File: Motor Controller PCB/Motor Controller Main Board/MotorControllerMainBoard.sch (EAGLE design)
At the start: 55 parts, among them T1 TEENSY_3.1_ALL_PINS

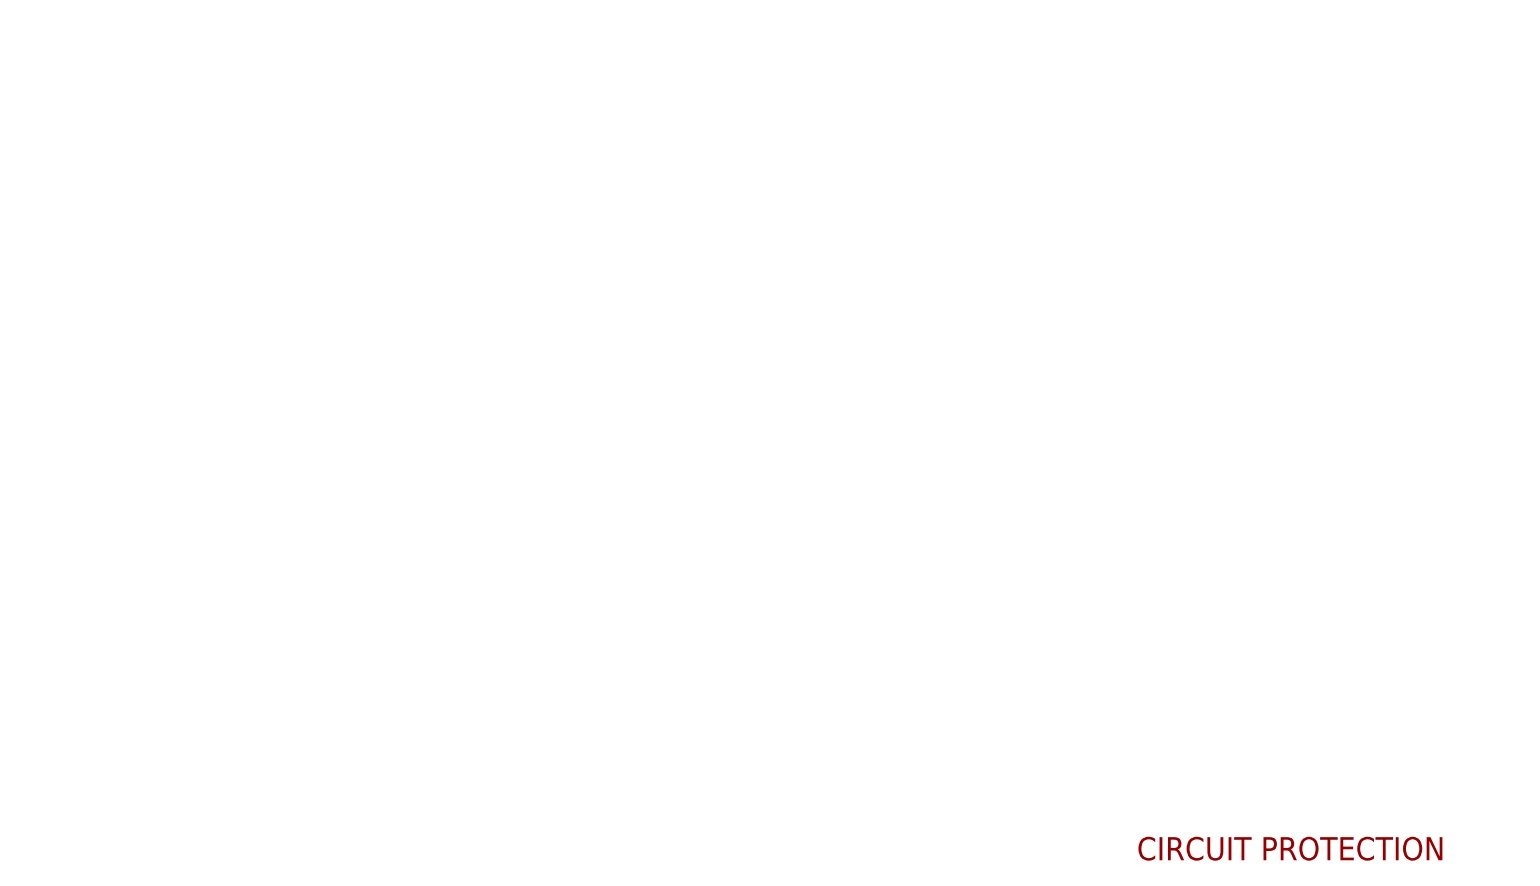
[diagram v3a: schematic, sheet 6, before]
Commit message: Added input filter Capacitors.
3.4mF of input capacitance that has very low effective series resistance
and inductance.
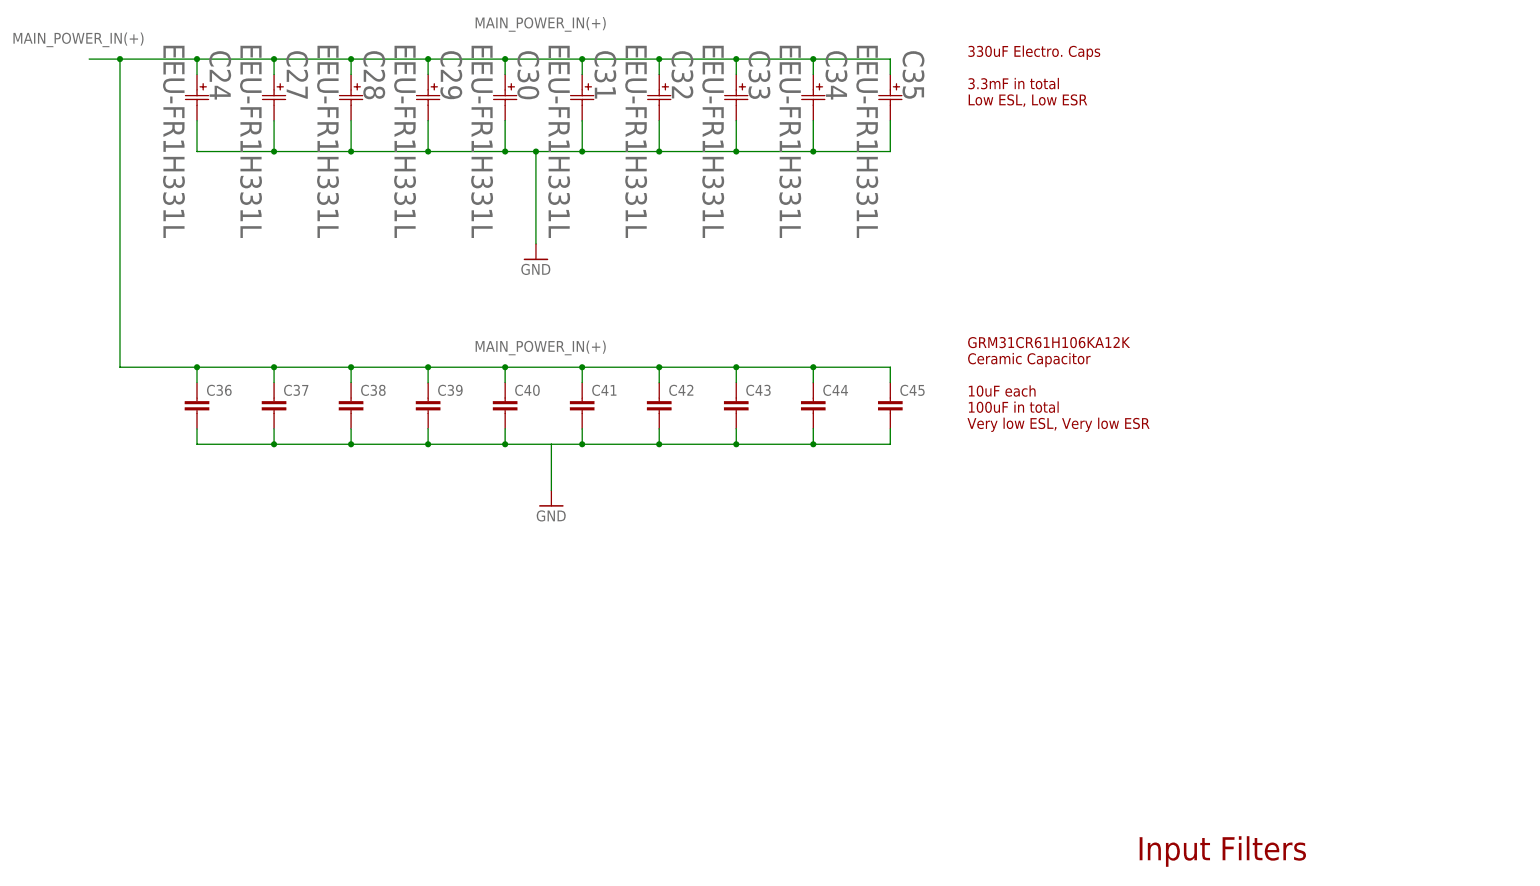
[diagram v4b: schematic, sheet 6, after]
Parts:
- added C24, C27, C28, C29, C30, C31, C32, C33, C34, C35: EEU-FR1H331L, MotorControllerEagleLibrary:EEU-FR1H331L
- added C36, C37, C38, C39, C40, C41, C42, C43, C44, C45: (no value), resistor:C-EUC1206
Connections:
- net GND: now also C24.22, C27.22, C28.22, C29.22, C30.22, C31.22, C32.22, C33.22, C34.22, C35.22, C36.2, C37.2, C38.2, C39.2, C40.2, C41.2, C42.2, C43.2, C44.2, C45.2
- net MAIN_POWER_IN(+): now also C24.11, C27.11, C28.11, C29.11, C30.11, C31.11, C32.11, C33.11, C34.11, C35.11, C36.1, C37.1, C38.1, C39.1, C40.1, C41.1, C42.1, C43.1, C44.1, C45.1
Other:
- note added: "330uF Electro. Caps 3.3mF in total Low ESL, Low ESR"
- note added: "GRM31CR61H106KA12K Ceramic Capacitor 10uF each 100uF in total Very low ESL, Very low ESR"
- note added: "Input Filters"
- note added: "On Board Filters"
- note removed: "CIRCUIT PROTECTION"
- note removed: "Circuit Protection - Overvoltage - Reverse Polarity"

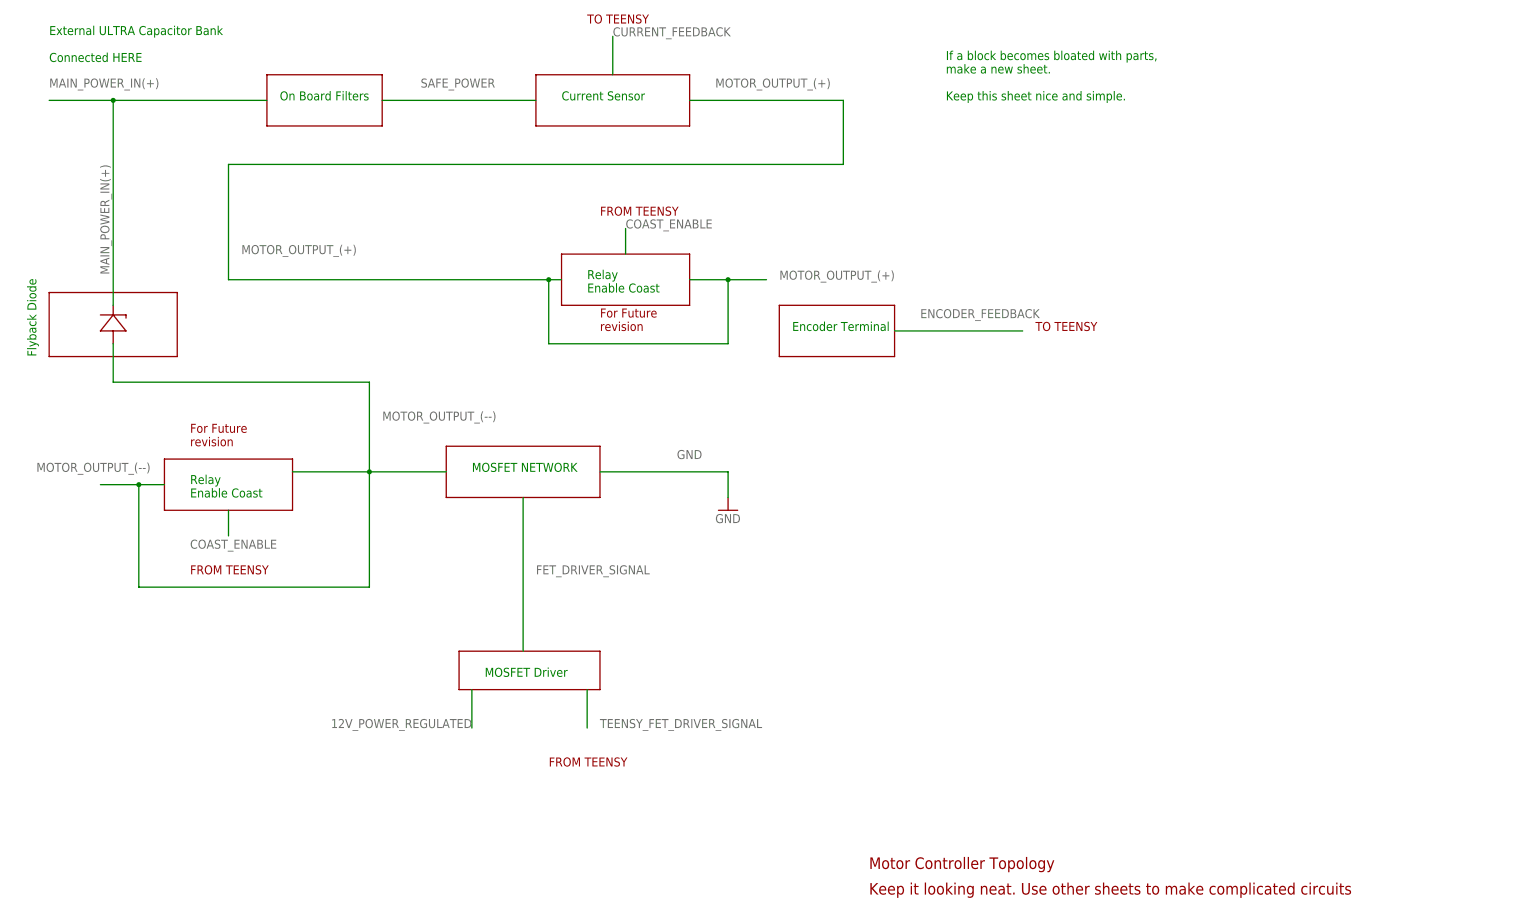
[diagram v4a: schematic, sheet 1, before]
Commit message: Added Screw Terminals to Schematic
-Added library for the screw terminal
-Added Power terminals and Motor terminals
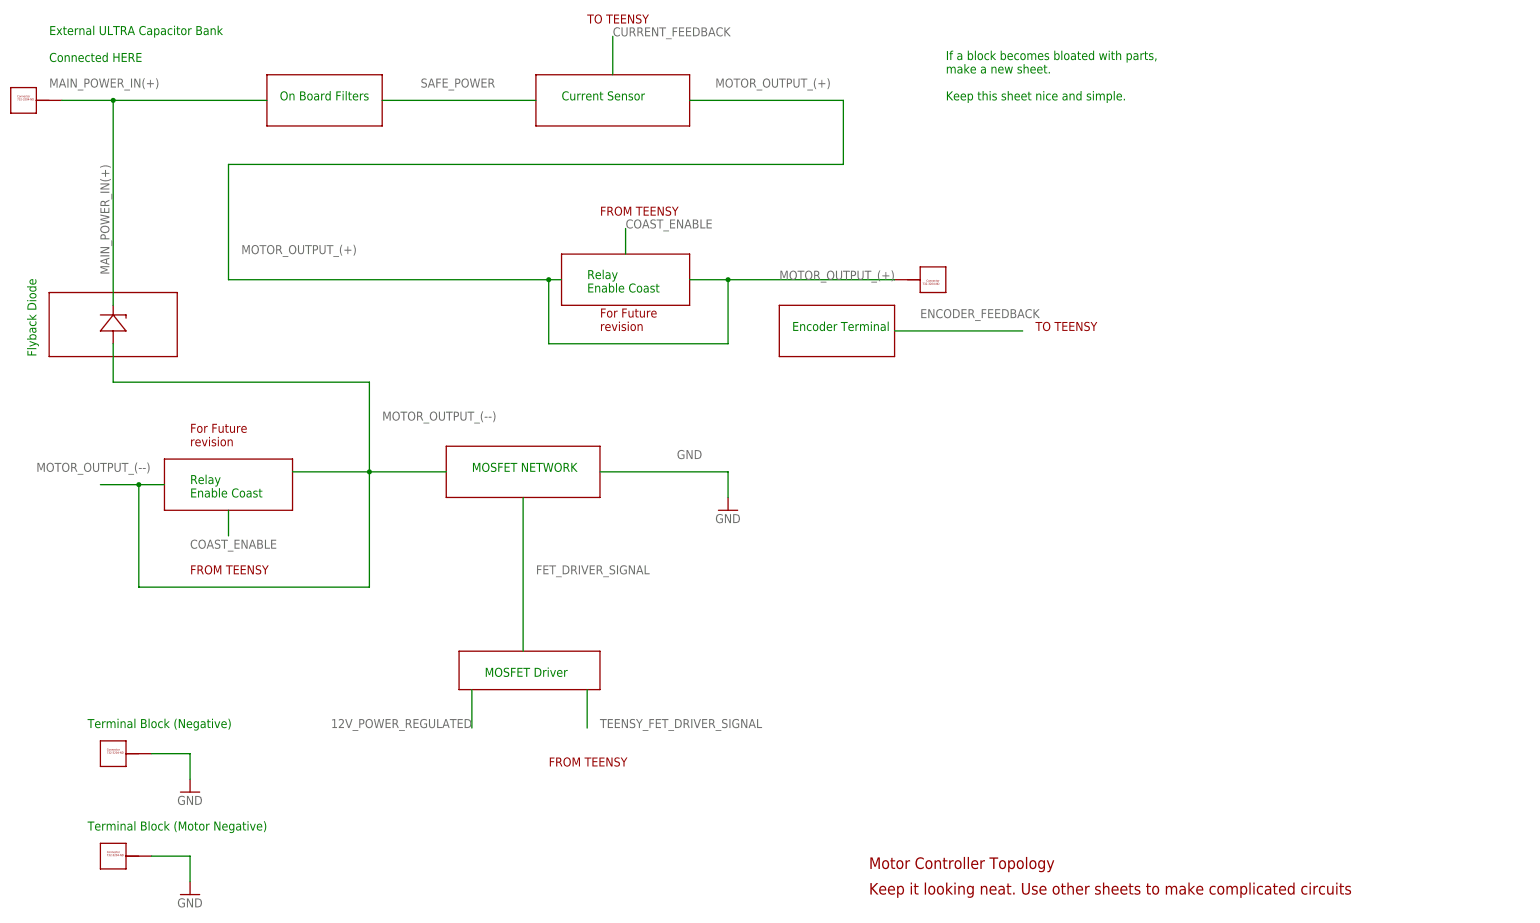
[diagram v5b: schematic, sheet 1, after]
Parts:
- added U$12, U$14, U$15, U$16: 732-3204-ND_CONNECTOR, Connector 732-3204:732-3204-ND_CONNECTOR
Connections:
- net GND: now also U$14.P$1
- net MAIN_POWER_IN(+): now also U$12.P$1
- net MOTOR_OUTPUT_(+): now also U$15.P$1
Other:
- note added: "Terminal Block (Motor Negative)"
- note added: "Terminal Block (Negative)"
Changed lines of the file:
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@@
 <part name="C45" library="resistor" deviceset="C-EU" device="C1206"/>
 <part name="GND25" library="SparkFun-Aesthetics" deviceset="GND" device=""/>
+<part name="U$12" library="Connector 732-3204" deviceset="732-3204-ND_CONNECTOR" device=""/>
+<part name="U$14" library="Connector 732-3204" deviceset="732-3204-ND_CONNECTOR" device=""/>
+<part name="GND26" library="E-P-008-R1.2" deviceset="GND" device=""/>
+<part name="U$15" library="Connector 732-3204" deviceset="732-3204-ND_CONNECTOR" device=""/>
+<part name="U$16" library="Connector 732-3204" deviceset="732-3204-ND_CONNECTOR" device=""/>
+<part name="GND27" library="E-P-008-R1.2" deviceset="GND" device=""/>
 </parts>
 <sheets>
@@
 <text x="121.92" y="137.16" size="1.778" layer="94">For Future
 revision</text>
+<text x="20.32" y="58.42" size="1.778" layer="91">Terminal Block (Negative)</text>
+<text x="20.32" y="38.1" size="1.778" layer="91">Terminal Block (Motor Negative)</text>
 </plain>
 <instances>
@@
 <instance part="GND1" gate="1" x="147.32" y="101.6"/>
 <instance part="U$5" gate="G$1" x="25.4" y="137.16" rot="R90"/>
+<instance part="U$12" gate="G$1" x="7.62" y="182.88"/>
+<instance part="U$14" gate="G$1" x="25.4" y="53.34"/>
+<instance part="GND26" gate="1" x="40.64" y="45.72"/>
+<instance part="U$15" gate="G$1" x="187.96" y="147.32" rot="R180"/>
+<instance part="U$16" gate="G$1" x="25.4" y="33.02"/>
+<instance part="GND27" gate="1" x="40.64" y="25.4"/>
 </instances>
 <busses>
@@
 <segment>
 <label x="22.86" y="170.18" size="1.778" layer="95" rot="R270"/>
-<wire x1="12.7" y1="182.88" x2="25.4" y2="182.88" width="0.1524" layer="91"/>
+<wire x1="15.24" y1="182.88" x2="25.4" y2="182.88" width="0.1524" layer="91"/>
 <label x="12.7" y="185.42" size="1.778" layer="95"/>
 <wire x1="25.4" y1="182.88" x2="55.88" y2="182.88" width="0.1524" layer="91"/>
@@
 <wire x1="25.4" y1="142.24" x2="25.4" y2="182.88" width="0.1524" layer="91"/>
 <pinref part="U$5" gate="G$1" pin="CATHODE"/>
+<pinref part="U$12" gate="G$1" pin="P$1"/>
 </segment>
 </net>
@@
 <wire x1="147.32" y1="109.22" x2="147.32" y2="104.14" width="0.1524" layer="91"/>
 <label x="137.16" y="111.76" size="1.778" layer="95"/>
+</segment>
+<segment>
+<pinref part="U$14" gate="G$1" pin="P$1"/>
+<wire x1="33.02" y1="53.34" x2="40.64" y2="53.34" width="0.1524" layer="91"/>
+<wire x1="40.64" y1="53.34" x2="40.64" y2="48.26" width="0.1524" layer="91"/>
+<pinref part="GND26" gate="1" pin="GND"/>
+</segment>
+<segment>
+<wire x1="33.02" y1="33.02" x2="40.64" y2="33.02" width="0.1524" layer="91"/>
+</segment>
+<segment>
+<wire x1="40.64" y1="33.02" x2="40.64" y2="27.94" width="0.1524" layer="91"/>
+<pinref part="GND27" gate="1" pin="GND"/>
 </segment>
 </net>
@@
 <wire x1="139.7" y1="147.32" x2="147.32" y2="147.32" width="0.1524" layer="91"/>
 <label x="157.48" y="147.32" size="1.778" layer="95"/>
-<wire x1="147.32" y1="147.32" x2="154.94" y2="147.32" width="0.1524" layer="91"/>
+<wire x1="147.32" y1="147.32" x2="180.34" y2="147.32" width="0.1524" layer="91"/>
 <wire x1="111.76" y1="147.32" x2="114.3" y2="147.32" width="0.1524" layer="91"/>
 <wire x1="111.76" y1="147.32" x2="111.76" y2="134.62" width="0.1524" layer="91"/>
@@
 <junction x="111.76" y="147.32"/>
 <wire x1="48.26" y1="147.32" x2="111.76" y2="147.32" width="0.1524" layer="91"/>
-</segment>
-</net>
+<pinref part="U$15" gate="G$1" pin="P$1"/>
+</segment>
+</net>

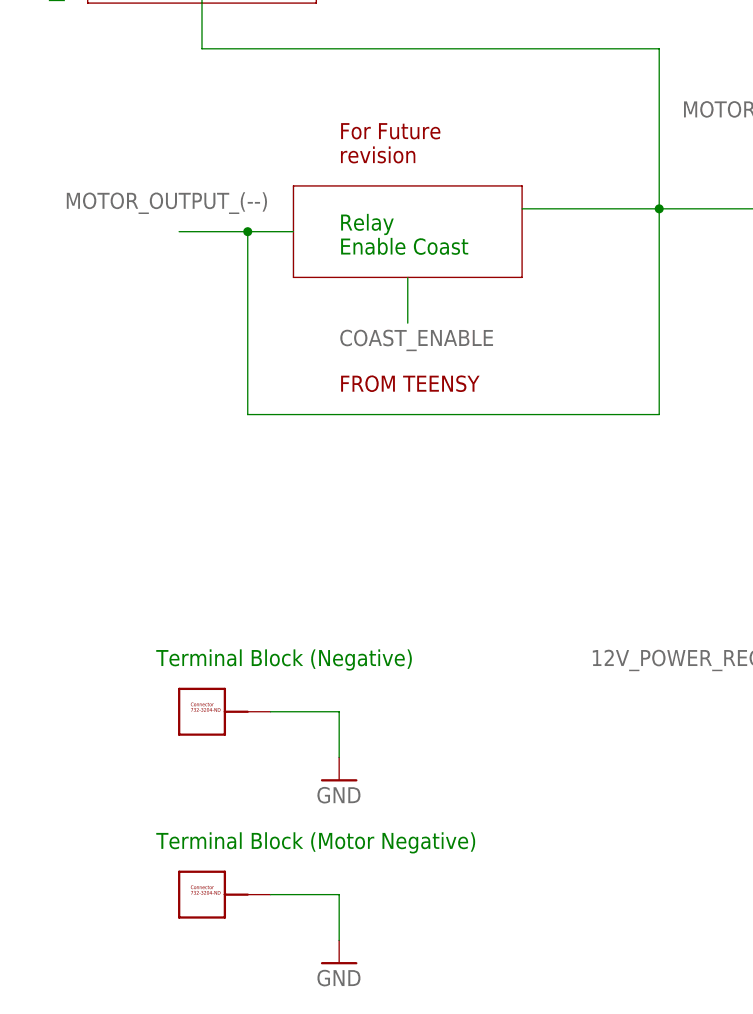
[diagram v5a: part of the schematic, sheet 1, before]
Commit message: Fixed mistake
-I put the screw terminal for the negative port for the motor in the
wrong spot
-Future update needs resistors on the gates of the FETs. I figure out
what size of resistor
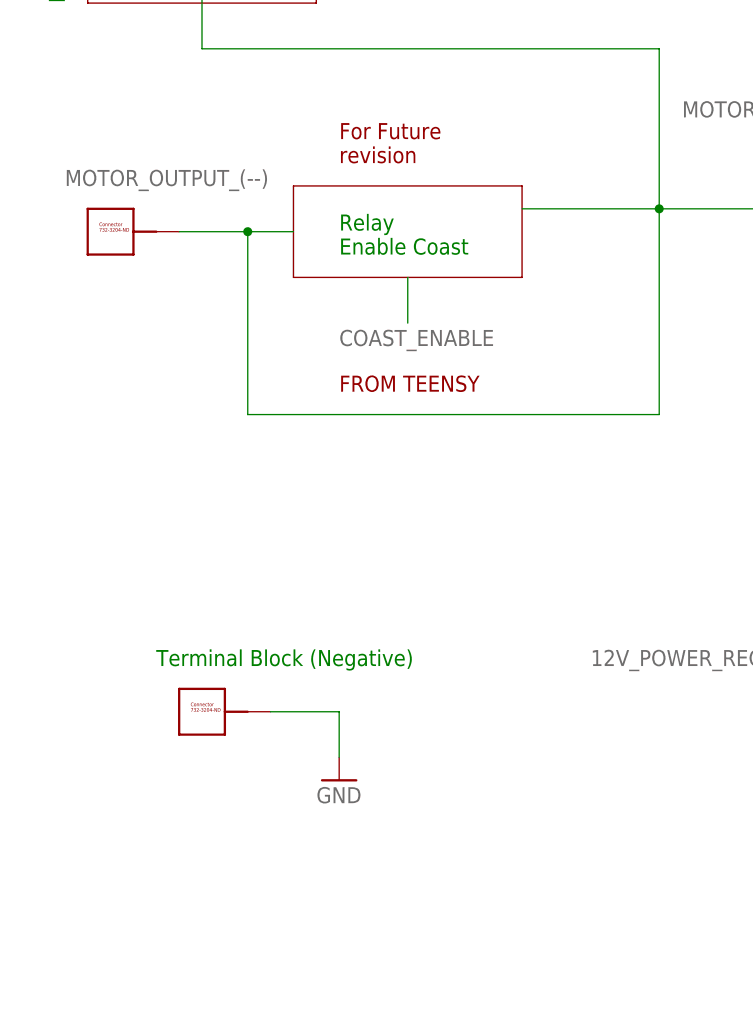
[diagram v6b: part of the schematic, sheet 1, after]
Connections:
- net MOTOR_OUTPUT_(--): now also U$16.P$1
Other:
- note removed: "Terminal Block (Motor Negative)"
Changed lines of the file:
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@@
 <part name="U$15" library="Connector 732-3204" deviceset="732-3204-ND_CONNECTOR" device=""/>
 <part name="U$16" library="Connector 732-3204" deviceset="732-3204-ND_CONNECTOR" device=""/>
-<part name="GND27" library="E-P-008-R1.2" deviceset="GND" device=""/>
 </parts>
 <sheets>
@@
 revision</text>
 <text x="20.32" y="58.42" size="1.778" layer="91">Terminal Block (Negative)</text>
-<text x="20.32" y="38.1" size="1.778" layer="91">Terminal Block (Motor Negative)</text>
 </plain>
 <instances>
@@
 <instance part="GND26" gate="1" x="40.64" y="45.72"/>
 <instance part="U$15" gate="G$1" x="187.96" y="147.32" rot="R180"/>
-<instance part="U$16" gate="G$1" x="25.4" y="33.02"/>
-<instance part="GND27" gate="1" x="40.64" y="25.4"/>
+<instance part="U$16" gate="G$1" x="15.24" y="106.68"/>
 </instances>
 <busses>
@@
 <segment>
 <wire x1="22.86" y1="106.68" x2="30.48" y2="106.68" width="0.1524" layer="91"/>
-<label x="10.16" y="109.22" size="1.778" layer="95"/>
+<label x="10.16" y="111.76" size="1.778" layer="95"/>
 <wire x1="30.48" y1="106.68" x2="35.56" y2="106.68" width="0.1524" layer="91"/>
 <wire x1="30.48" y1="106.68" x2="30.48" y2="86.36" width="0.1524" layer="91"/>
@@
 <label x="78.74" y="119.38" size="1.778" layer="95"/>
 <pinref part="U$5" gate="G$1" pin="ANODE"/>
+<pinref part="U$16" gate="G$1" pin="P$1"/>
 </segment>
 </net>
@@
 <pinref part="GND26" gate="1" pin="GND"/>
 </segment>
-<segment>
-<wire x1="33.02" y1="33.02" x2="40.64" y2="33.02" width="0.1524" layer="91"/>
-</segment>
-<segment>
-<wire x1="40.64" y1="33.02" x2="40.64" y2="27.94" width="0.1524" layer="91"/>
-<pinref part="GND27" gate="1" pin="GND"/>
-</segment>
 </net>
